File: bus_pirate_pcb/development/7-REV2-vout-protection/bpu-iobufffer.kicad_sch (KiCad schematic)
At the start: 45 parts, among them J301 Conn_01x10, J302 Conn_01x09, U14 SP3002-04JTG, U15 SP3002-04JTG, U301 AiP74LVC1T45GC363.TR, U302 AiP74LVC1T45GC363.TR, U303 AiP74LVC1T45GC363.TR, U304 AiP74LVC1T45GC363.TR, U305 AiP74LVC1T45GC363.TR, U306 AiP74LVC1T45GC363.TR, U307 AiP74LVC1T45GC363.TR, U308 AiP74LVC1T45GC363.TR

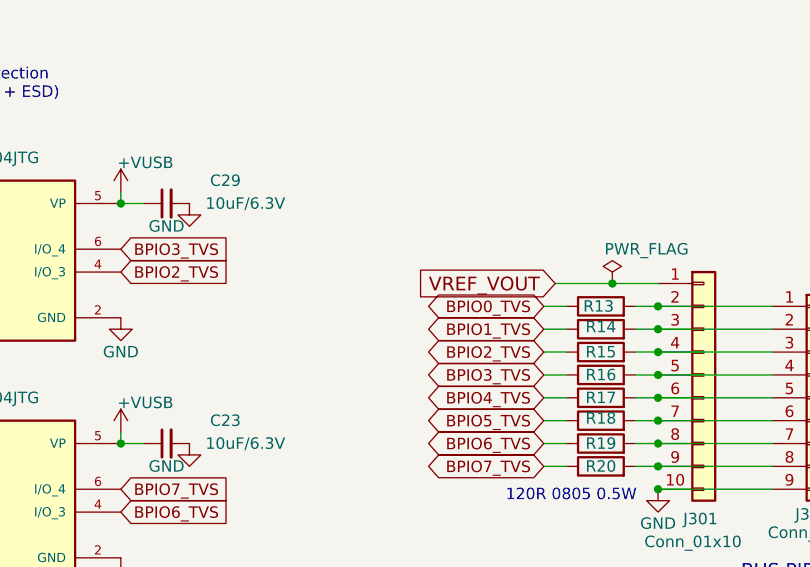
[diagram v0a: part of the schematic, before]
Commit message: BP 7R2 VOUT protection
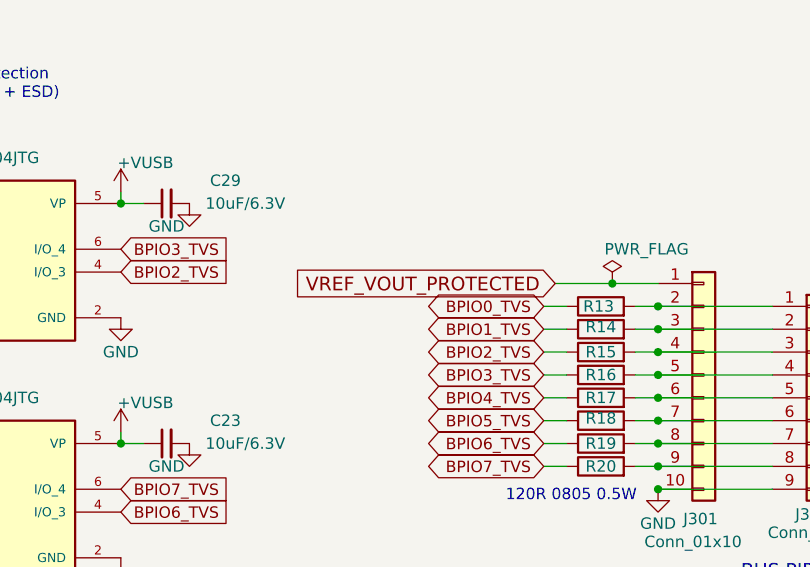
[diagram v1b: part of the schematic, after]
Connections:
- net VREF_VOUT: no longer J301.1 (Pin_1)
- new net VREF_VOUT_PROTECTED: J301.1 (Pin_1)
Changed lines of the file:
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@@
 		)
 	)
-	(global_label "VREF_VOUT"
+	(global_label "VREF_VOUT_PROTECTED"
 		(shape input)
 		(at 115.57 157.48 180)
